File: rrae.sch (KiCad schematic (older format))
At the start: 0 parts

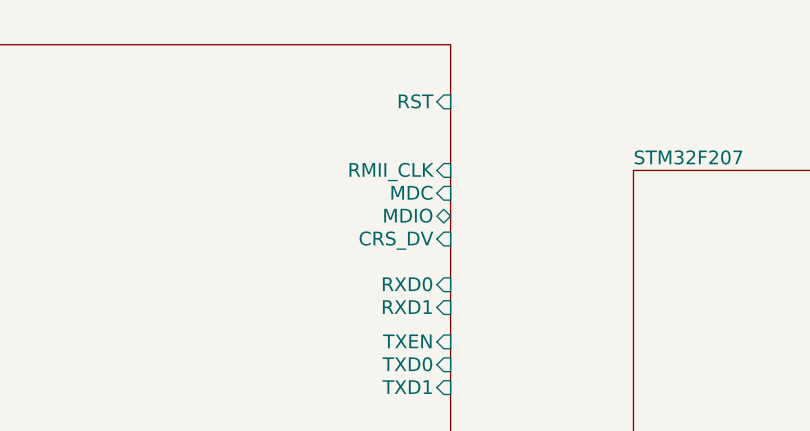
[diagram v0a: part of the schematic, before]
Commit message: Made the Clock Source for the Phy. Removed the 50MHz OSC from the notes page.
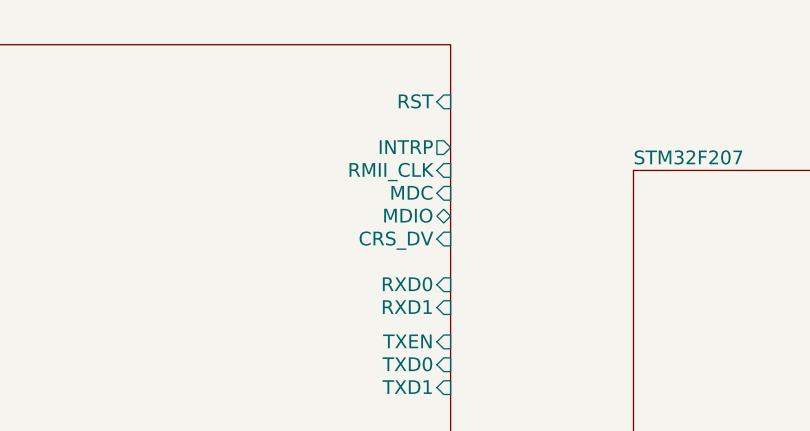
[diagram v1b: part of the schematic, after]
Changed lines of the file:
@@
-EESchema Schematic File Version 2  date 9/24/2011 1:49:25 PM
+EESchema Schematic File Version 2  date 9/26/2011 6:52:56 PM
 LIBS:power
 LIBS:device
@@
 $Descr A4 11700 8267
 encoding utf-8
-Sheet 1 5
+Sheet 1 4
 Title ""
-Date "24 sep 2011"
+Date "26 sep 2011"
 Rev ""
 Comp ""
@@
 F10 "MDC" I R 4250 2150 60
 F11 "MDIO" B R 4250 2250 60
+F12 "INTRP" O R 4250 1950 60
 $EndSheet
 $Sheet

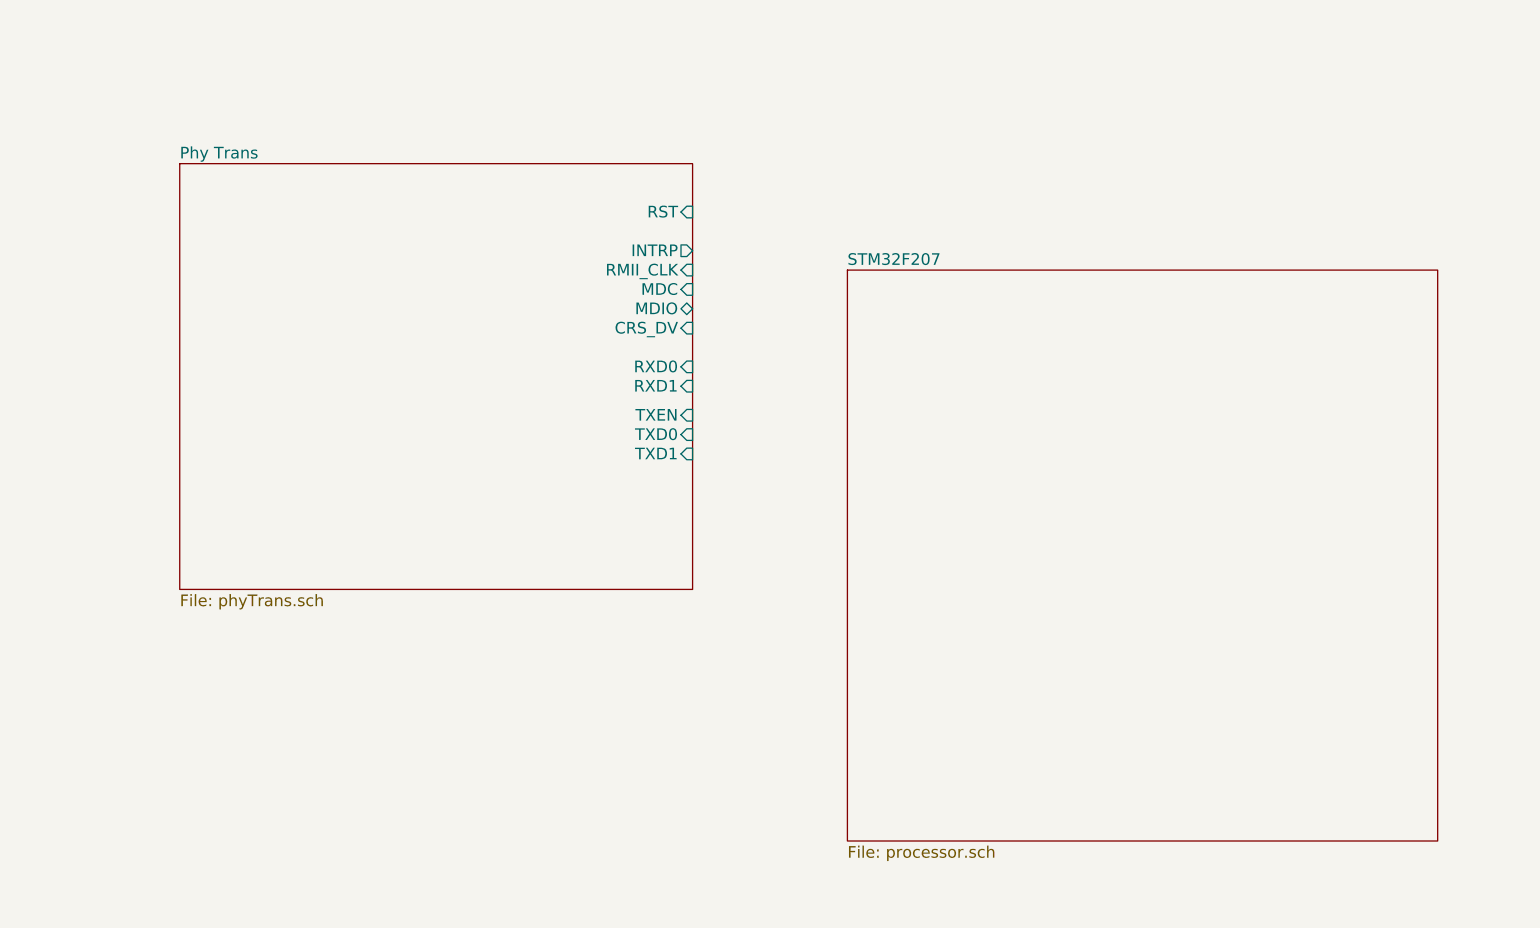
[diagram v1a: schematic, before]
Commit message: Made the connections in the main schematic from the ETH PHY to the Processor
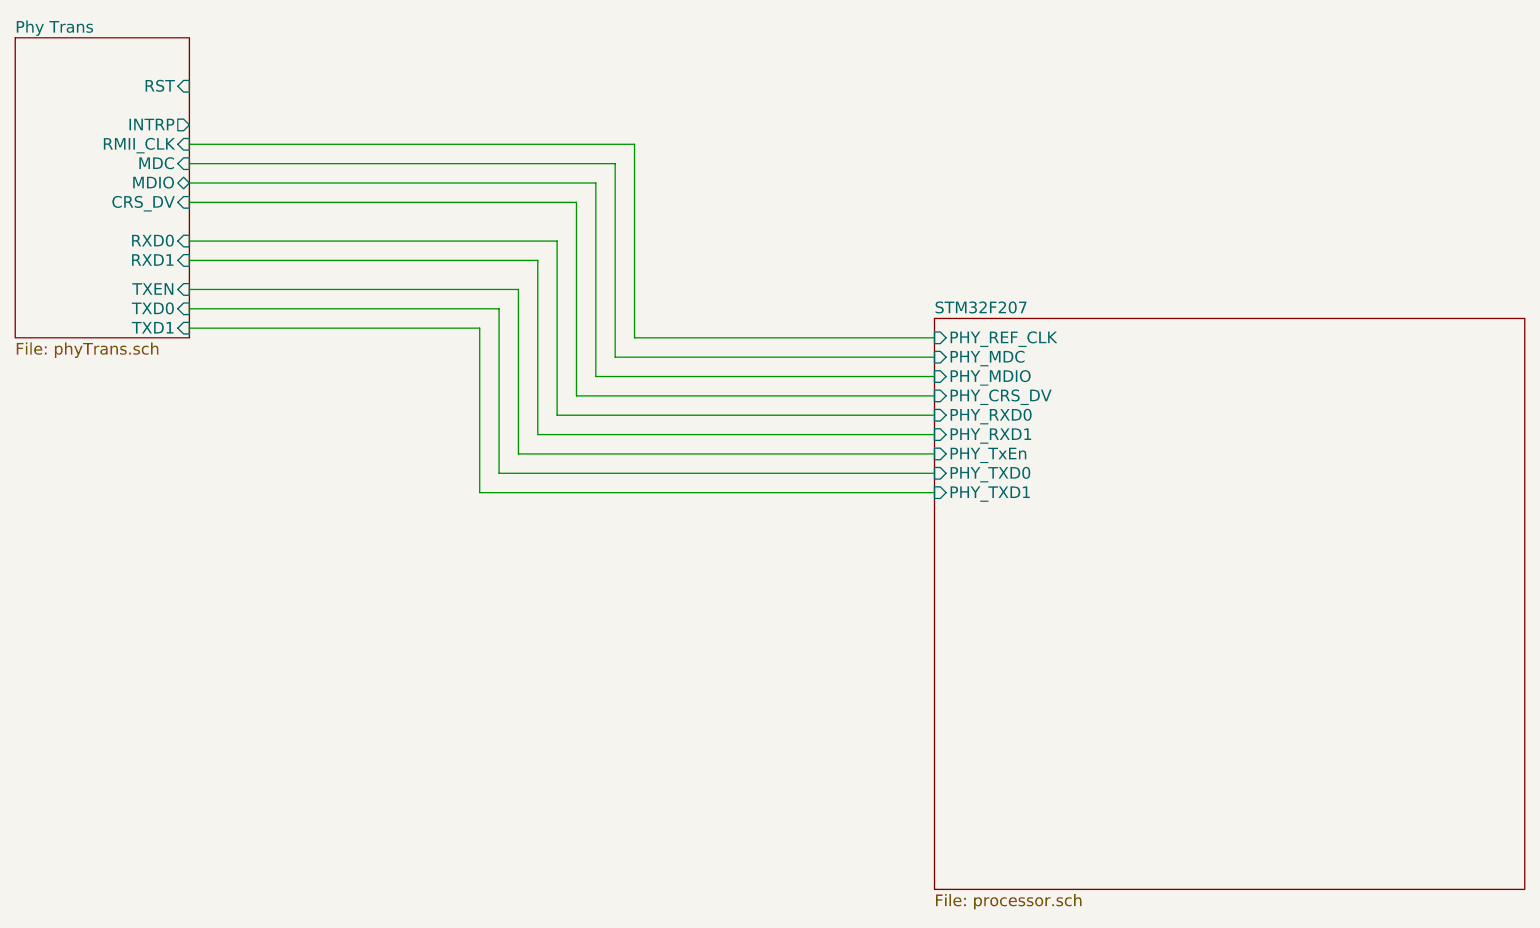
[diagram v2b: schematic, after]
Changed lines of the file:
@@
-EESchema Schematic File Version 2  date 9/26/2011 6:52:56 PM
+EESchema Schematic File Version 2  date 9/26/2011 8:30:03 PM
 LIBS:power
 LIBS:device
@@
 Sheet 1 4
 Title ""
-Date "26 sep 2011"
+Date "27 sep 2011"
 Rev ""
 Comp ""
@@
 Comment4 ""
 $EndDescr
+Wire Wire Line
+	5500 3200 3150 3200
+Wire Wire Line
+	3150 3200 3150 2350
+Wire Wire Line
+	3150 2350 1650 2350
+Wire Wire Line
+	5500 3000 3350 3000
+Wire Wire Line
+	3350 3000 3350 2150
+Wire Wire Line
+	3350 2150 1650 2150
+Wire Wire Line
+	5500 2800 3550 2800
+Wire Wire Line
+	3550 2800 3550 1900
+Wire Wire Line
+	3550 1900 1650 1900
+Wire Wire Line
+	1650 1500 3850 1500
+Wire Wire Line
+	3850 1500 3850 2500
+Wire Wire Line
+	3850 2500 5500 2500
+Wire Wire Line
+	1650 1400 3950 1400
+Wire Wire Line
+	3950 1400 3950 2400
+Wire Wire Line
+	3950 2400 5500 2400
+Wire Wire Line
+	1650 1600 3750 1600
+Wire Wire Line
+	3750 1600 3750 2600
+Wire Wire Line
+	3750 2600 5500 2600
+Wire Wire Line
+	1650 1700 3650 1700
+Wire Wire Line
+	3650 1700 3650 2700
+Wire Wire Line
+	3650 2700 5500 2700
+Wire Wire Line
+	5500 2900 3450 2900
+Wire Wire Line
+	3450 2900 3450 2000
+Wire Wire Line
+	3450 2000 1650 2000
+Wire Wire Line
+	5500 3100 3250 3100
+Wire Wire Line
+	3250 3100 3250 2250
+Wire Wire Line
+	3250 2250 1650 2250
 $Sheet
-S 1600 1500 2650 2200
+S 750  850  900  1550
 U 4E7A8C23
 F0 "Phy Trans" 60
 F1 "phyTrans.sch" 60
-F2 "CRS_DV" I R 4250 2350 60
-F3 "RXD1" I R 4250 2650 60
-F4 "RXD0" I R 4250 2550 60
-F5 "TXD1" I R 4250 3000 60
-F6 "TXD0" I R 4250 2900 60
-F7 "TXEN" I R 4250 2800 60
-F8 "RST" I R 4250 1750 60
-F9 "RMII_CLK" I R 4250 2050 60
-F10 "MDC" I R 4250 2150 60
-F11 "MDIO" B R 4250 2250 60
-F12 "INTRP" O R 4250 1950 60
+F2 "CRS_DV" I R 1650 1700 60
+F3 "RXD1" I R 1650 2000 60
+F4 "RXD0" I R 1650 1900 60
+F5 "TXD1" I R 1650 2350 60
+F6 "TXD0" I R 1650 2250 60
+F7 "TXEN" I R 1650 2150 60
+F8 "RST" I R 1650 1100 60
+F9 "RMII_CLK" I R 1650 1400 60
+F10 "MDC" I R 1650 1500 60
+F11 "MDIO" B R 1650 1600 60
+F12 "INTRP" O R 1650 1300 60
 $EndSheet
 $Sheet
-S 5050 2050 3050 2950
+S 5500 2300 3050 2950
 U 4E7DF058
 F0 "STM32F207" 60
 F1 "processor.sch" 60
+F2 "PHY_REF_CLK" I L 5500 2400 60
+F3 "PHY_MDIO" I L 5500 2600 60
+F4 "PHY_MDC" I L 5500 2500 60
+F5 "PHY_CRS_DV" I L 5500 2700 60
+F6 "PHY_TxEn" I L 5500 3000 60
+F7 "PHY_RXD1" I L 5500 2900 60
+F8 "PHY_RXD0" I L 5500 2800 60
+F9 "PHY_TXD1" I L 5500 3200 60
+F10 "PHY_TXD0" I L 5500 3100 60
 $EndSheet
 $EndSCHEMATC

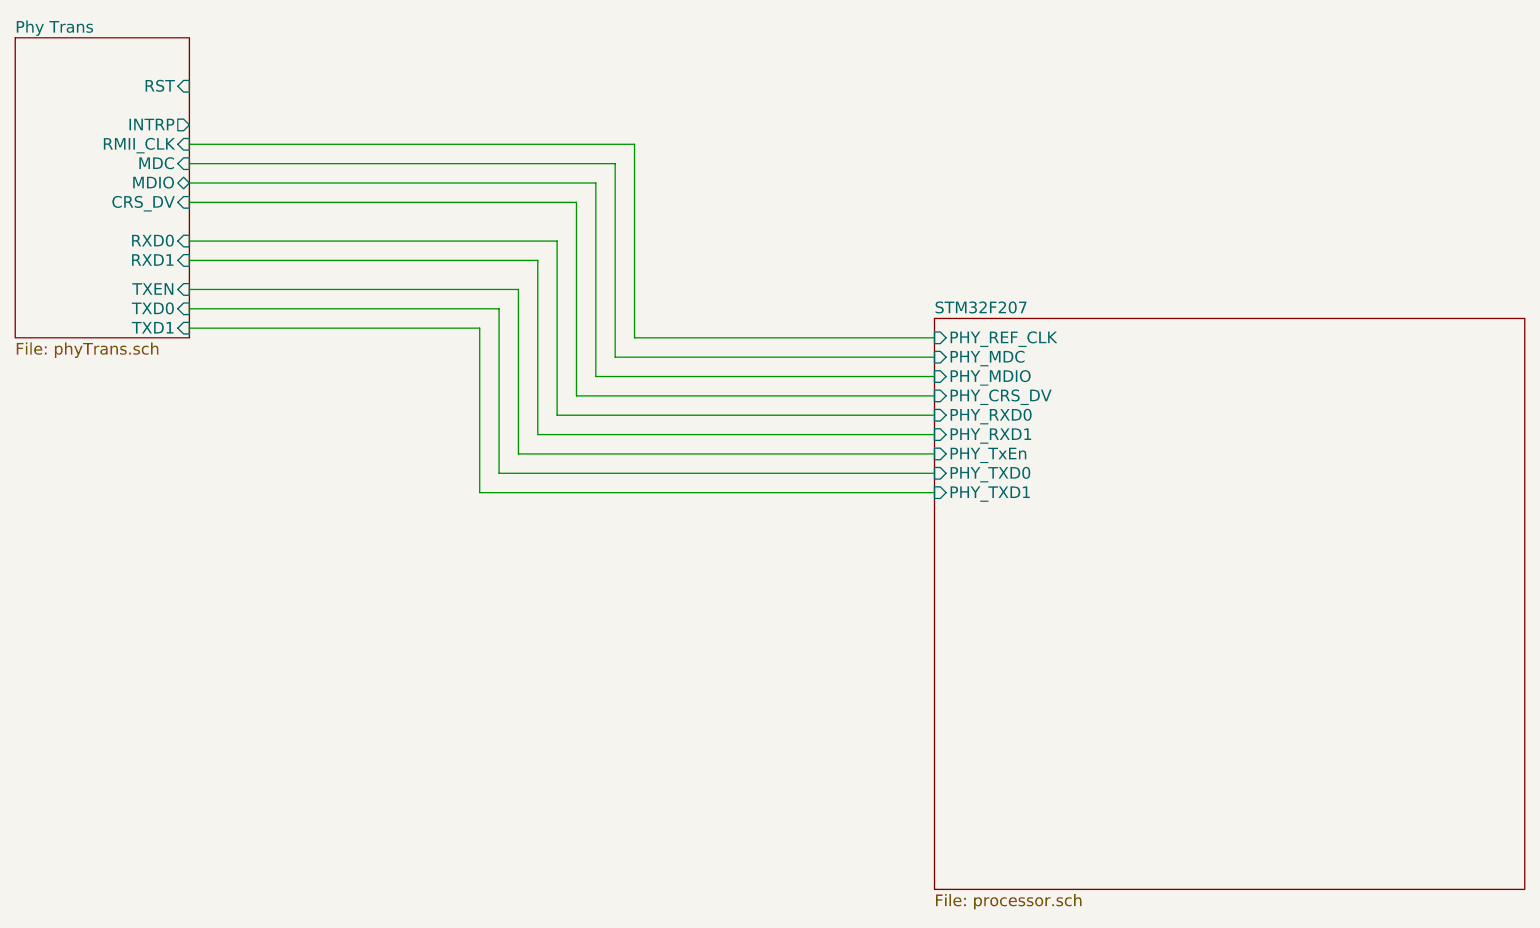
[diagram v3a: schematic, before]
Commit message: Created the reset scheatic and connected it.  Still need to find a pin to do the soft reset.
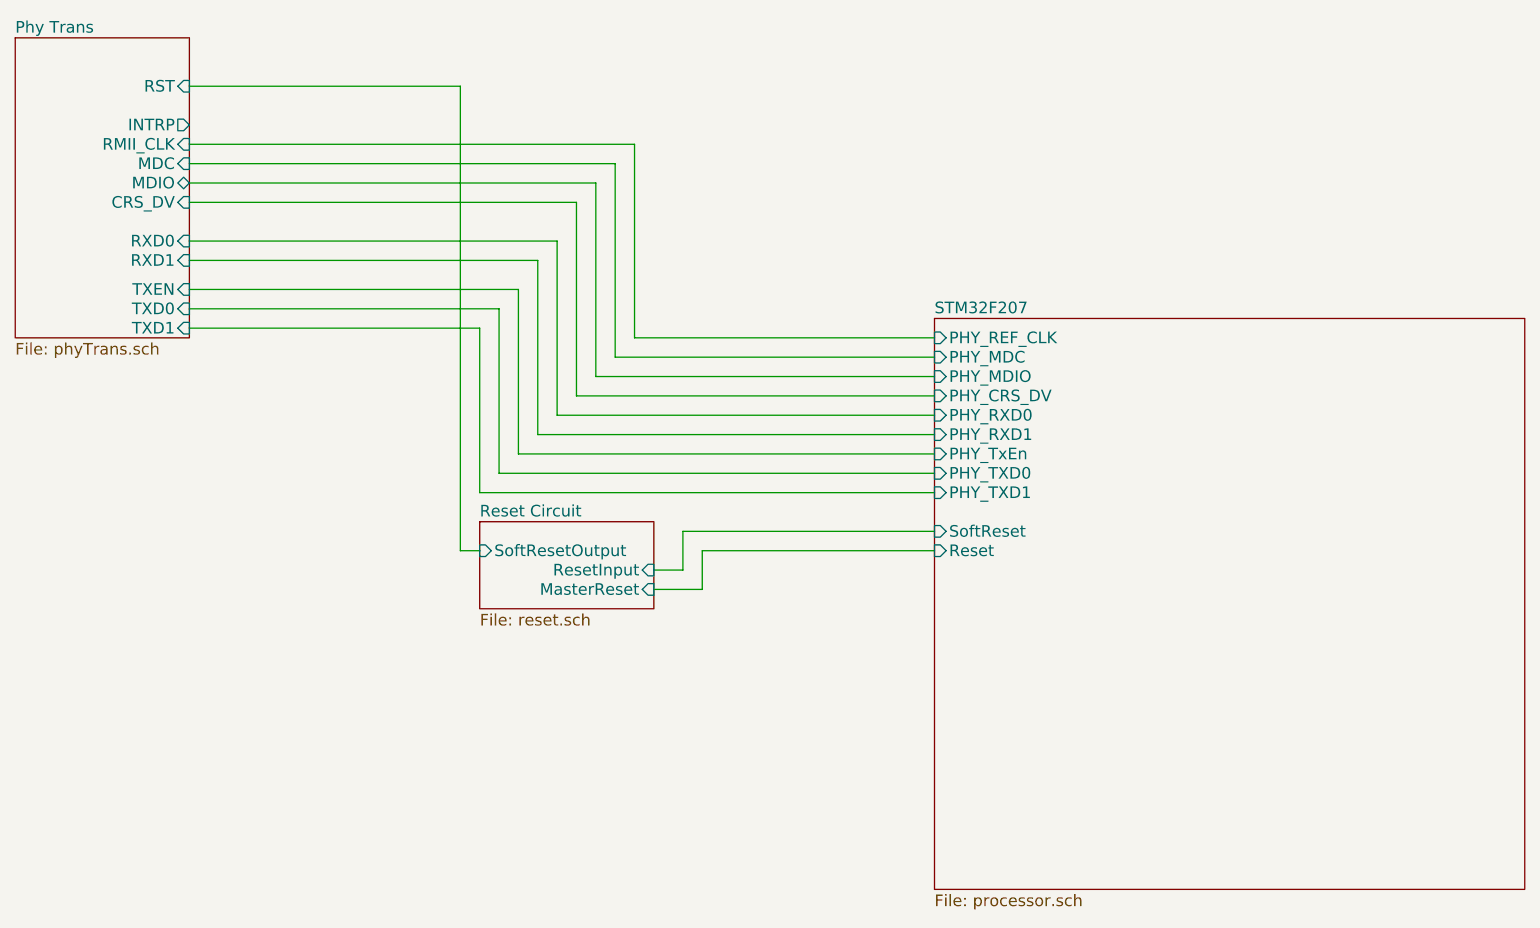
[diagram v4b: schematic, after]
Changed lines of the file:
@@
-EESchema Schematic File Version 2  date 9/26/2011 11:46:43 PM
+EESchema Schematic File Version 2  date 9/27/2011 12:42:11 AM
 LIBS:power
 LIBS:device
@@
 $Descr A4 11700 8267
 encoding utf-8
-Sheet 1 5
+Sheet 1 7
 Title ""
 Date "27 sep 2011"
@@
 Comment4 ""
 $EndDescr
+Wire Wire Line
+	3150 3500 3050 3500
+Wire Wire Line
+	3050 3500 3050 1100
+Wire Wire Line
+	3050 1100 1650 1100
+Wire Wire Line
+	5500 3400 4200 3400
+Wire Wire Line
+	4200 3400 4200 3600
+Wire Wire Line
+	4200 3600 4050 3600
 Wire Wire Line
 	5500 3200 3150 3200
@@
 Wire Wire Line
 	3250 2250 1650 2250
+Wire Wire Line
+	4050 3700 4300 3700
+Wire Wire Line
+	4300 3700 4300 3500
+Wire Wire Line
+	4300 3500 5500 3500
+$Sheet
+S 3150 3350 900  450
+U 4E815C62
+F0 "Reset Circuit" 60
+F1 "reset.sch" 60
+F2 "ResetInput" I R 4050 3600 60
+F3 "SoftResetOutput" I L 3150 3500 60
+F4 "MasterReset" I R 4050 3700 60
+$EndSheet
 $Sheet
 S 750  850  900  1550
@@
 F9 "PHY_TXD1" I L 5500 3200 60
 F10 "PHY_TXD0" I L 5500 3100 60
+F11 "SoftReset" I L 5500 3400 60
+F12 "Reset" I L 5500 3500 60
 $EndSheet
 $EndSCHEMATC
